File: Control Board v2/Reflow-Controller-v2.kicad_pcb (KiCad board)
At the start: 6 copper layers, 102.5 x 108 mm, 52 parts, among them J1 1366005, J2 1366005, J3 ISP, J4 Conn_01x05, J5 Conn_01x14, J6 Conn_01x04, Q1 SQ2315CES-T1_GE3, Q2 BSS127 H6327, SW1 SW_SPST, SW2 SW_Push, U2 MOC3083S-TA1, U5 ATmega328PB-A, Y2 16MHz

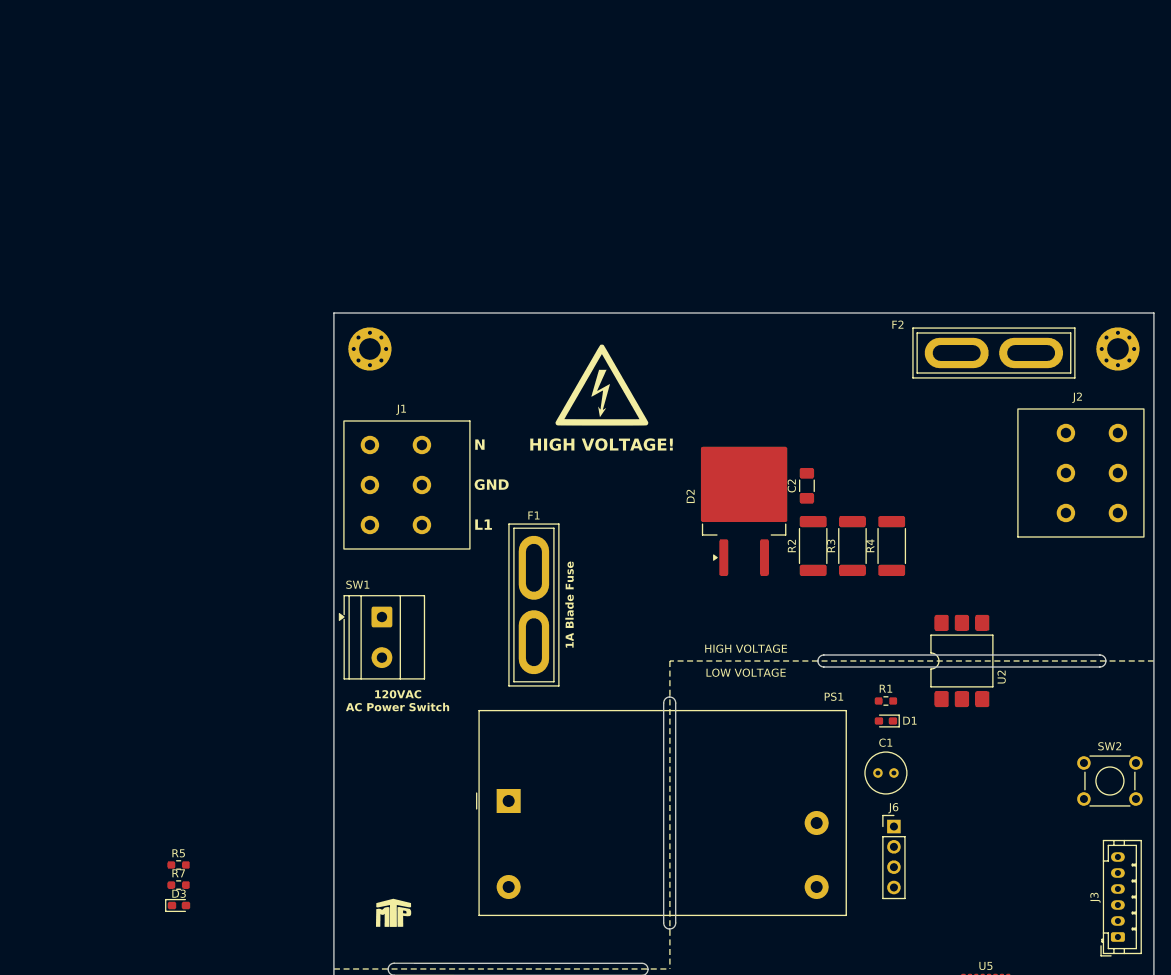
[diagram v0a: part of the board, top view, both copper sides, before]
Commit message: add silkscreen to bottom of board
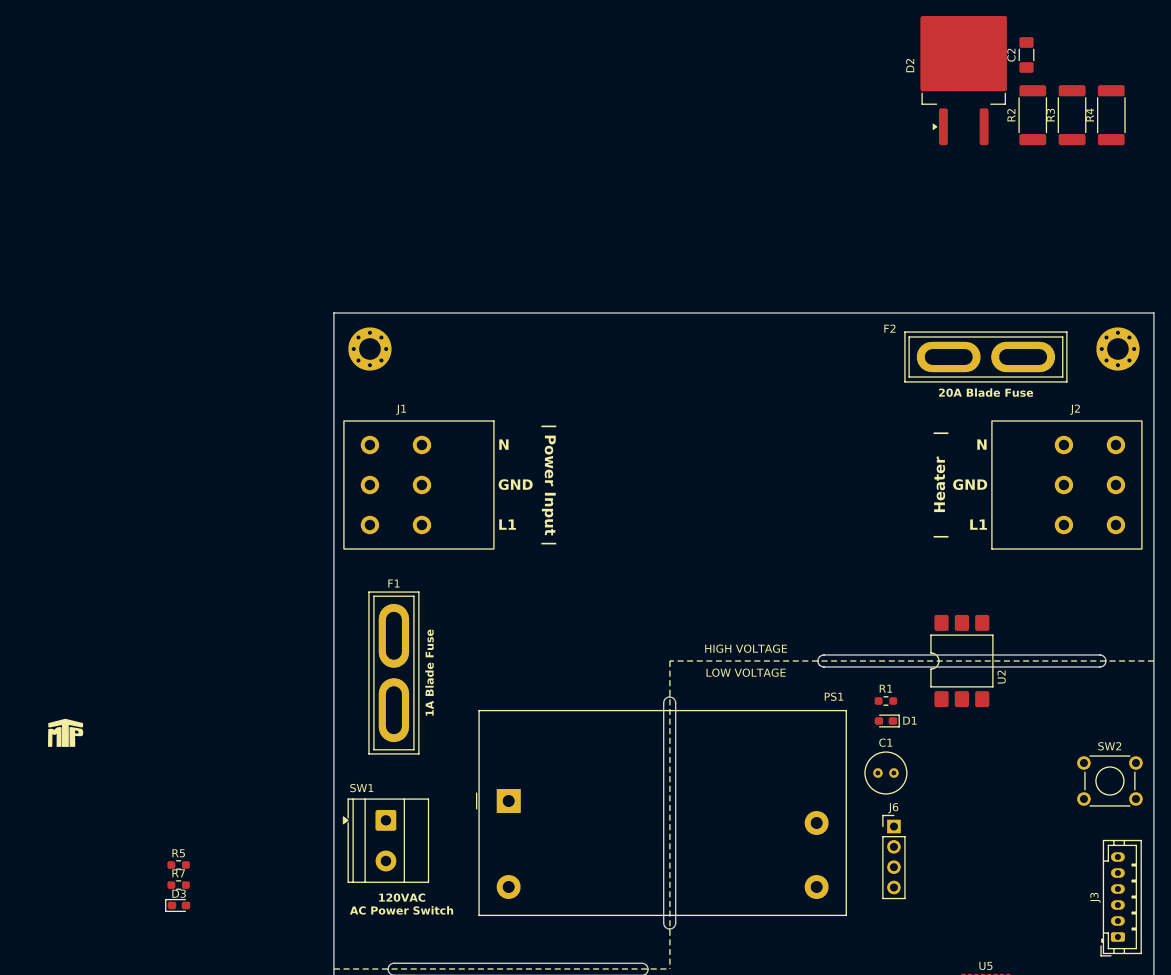
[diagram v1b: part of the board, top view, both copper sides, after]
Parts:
- G***: moved to B.Cu
- moved R4 60.4 mm to (225.7, -5.72)
- moved C2 60.4 mm to (215.1, -13.3)
- moved R2 60.4 mm to (215.9, -5.72)
- moved R3 60.4 mm to (220.8, -5.72)
- moved D2 60.4 mm to (207.2, -11.9)
- moved REF** 46.8 mm to (95.0, 72.0)
- moved SW1 25.4 mm to (135.0, 82.4)
- moved F1 19.5 mm to (136.0, 59.4)
- moved G*** 19.3 mm to (180.0, 35.0), turned to 180 degrees
- moved J2 1.52 mm to (213.0, 40.5)
- moved F2 1.12 mm to (205.3, 24.5)
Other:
- board text added: "20A Blade Fuse"
- board text added: "HIGH VOLTAGE! 120 VAC"
- board text added: "| Heater |"
- board text added: "| Power Input |"
- board text removed: "HIGH VOLTAGE!"

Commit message: change to glass fuses instead of blade fuses
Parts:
- F1: footprint Fuse:Fuse_Blade_ATO_directSolder -> Fuse:Fuseholder_Clip-5x20mm_Bel_FC-203-22_Lateral_P17.80x5.00mm_D1.17mm_Horizontal
- F2: footprint Fuse:Fuse_Blade_ATO_directSolder -> Fuse:Fuseholder_Clip-6.3x32mm_Littelfuse_122_Inline_P34.21x7.62mm_D2.54mm_Horizontal
- moved C6 185.6 mm to (219.0, 106.1)
- moved C7 185.6 mm to (219.0, 108.0)
- moved C8 185.6 mm to (219.0, 110.0)
- moved C9 185.6 mm to (219.0, 112.0)
- moved R14 185.6 mm to (217.4, 122.0)
- moved Y2 185.6 mm to (218.6, 118.7)
- moved BZ1 159.6 mm to (211.5, 90.0)
- moved TP3 120.4 mm to (179.9, 99.0)
- moved TP4 120.4 mm to (179.9, 102.5)
- moved TP7 120.4 mm to (187.0, 99.0)
- moved TP8 120.4 mm to (187.0, 102.5)
- moved D4 120.4 mm to (176.8, 105.6)
- moved R8 120.4 mm to (181.1, 105.5)
- moved TP1 120.4 mm to (176.3, 99.0)
- moved TP2 120.4 mm to (176.3, 102.5)
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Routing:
- net L1: track 0.00 -> 33.6 mm
- net /Project Architecture/AC-DC Power Supply/L1_F1_SW: track 0.00 -> 16.7 mm
- net /Project Architecture/AC-DC Power Supply/L1_F1: track 0.00 -> 15.1 mm
- net GNDPWR: track 0.00 -> 13.0 mm
- net LN: track 0.00 -> 6.50 mm
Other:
- copper layers 6 -> 4
- board text added: "1A Fuse"
- board text added: "20A Fuse"
- board text removed: "1A Blade Fuse"
- board text removed: "20A Blade Fuse"

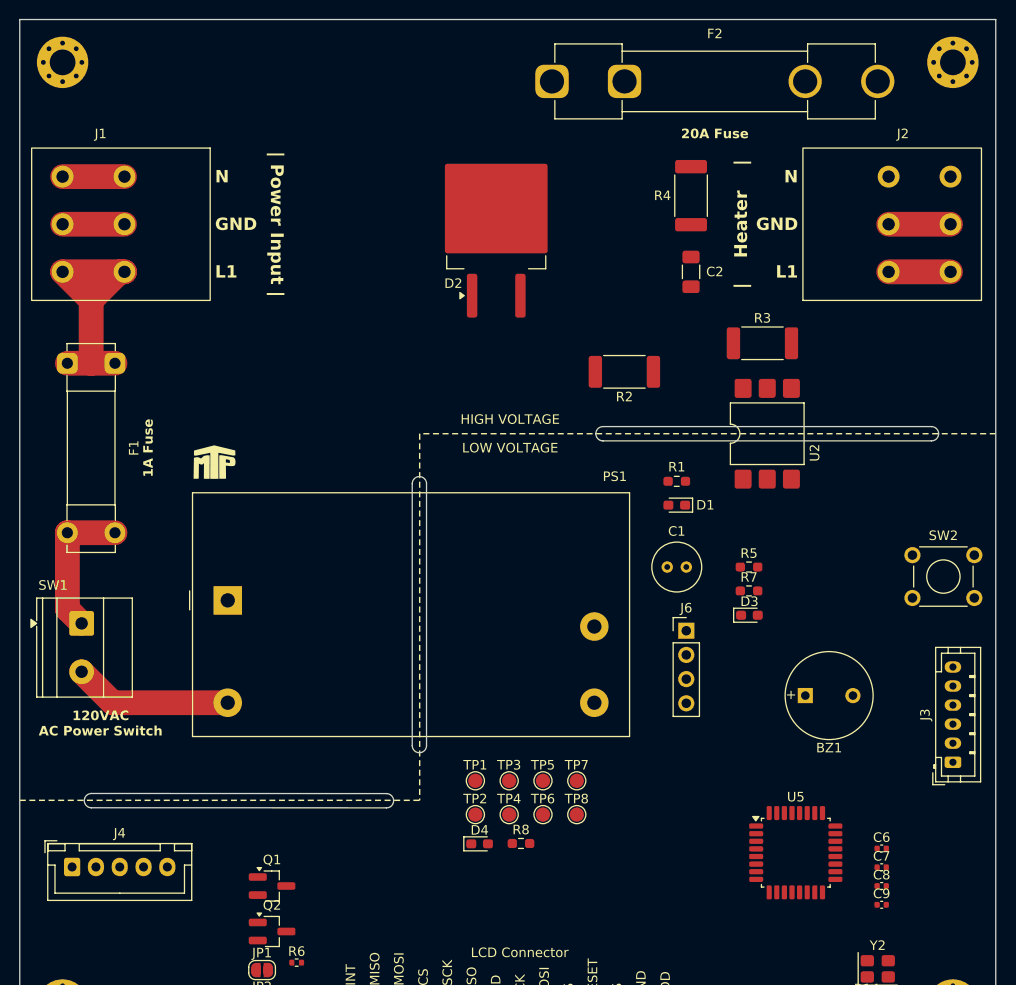
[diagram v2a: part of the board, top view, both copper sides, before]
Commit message: got most HV routed
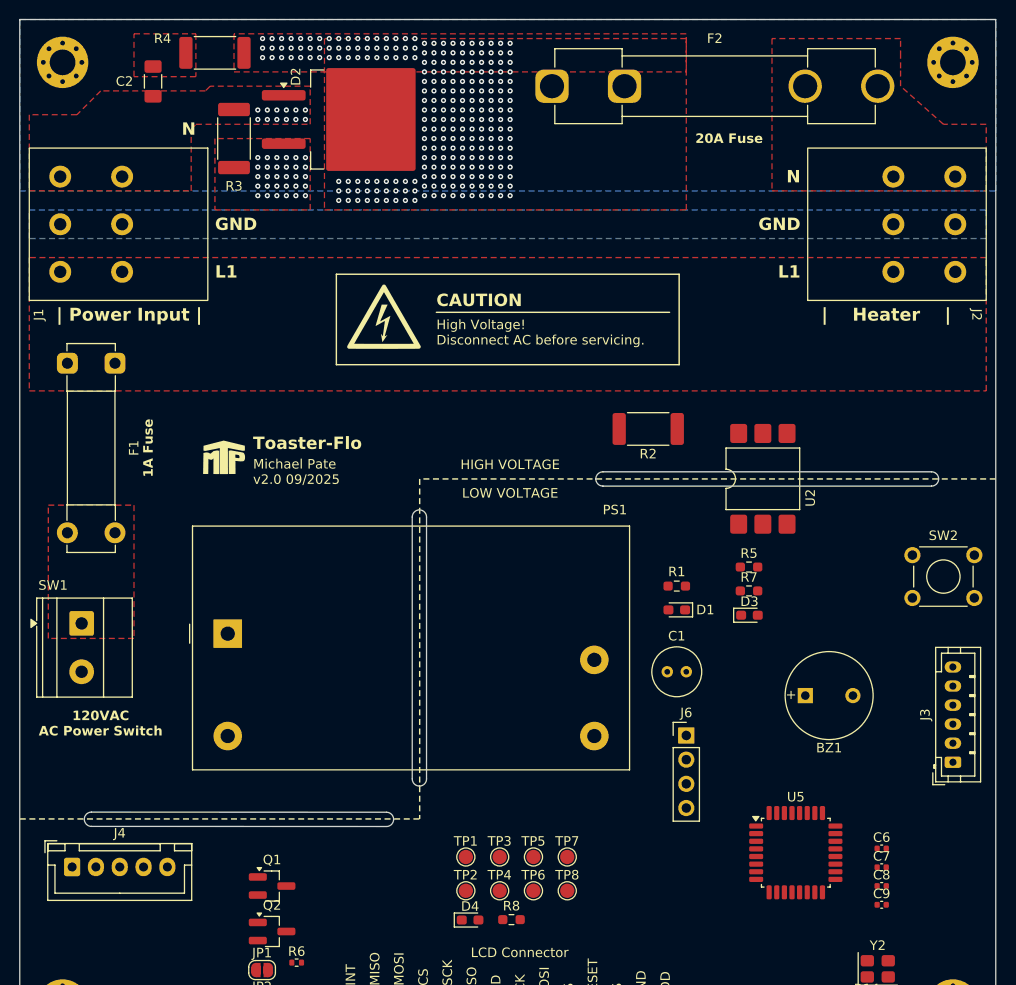
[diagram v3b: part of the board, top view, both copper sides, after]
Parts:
- added G***: LOGO, LOGO, F.Cu at (166.8, 50.2)
- moved C2 59.9 mm to (142.5, 25.5)
- moved R3 59.5 mm to (151.0, 31.5), turned to -90 degrees
- moved R4 52.2 mm to (149.0, 22.5), turned to 0 degrees
- moved D2 18.2 mm to (163.9, 29.5), turned to 0 degrees
- moved C1 11.0 mm to (196.5, 87.5)
- moved D1 11.0 mm to (197.5, 81.0)
- moved G*** 11.0 mm to (180.0, 46.0)
- moved J6 11.0 mm to (198.5, 94.2)
- moved R1 11.0 mm to (197.5, 78.5)
- moved D4 8.06 mm to (175.8, 113.6)
- moved R8 8.06 mm to (180.1, 113.5)
- moved TP1 8.06 mm to (175.3, 107.0)
- moved TP2 8.06 mm to (175.3, 110.5)
- moved TP3 8.06 mm to (178.9, 107.0)
- moved TP4 8.06 mm to (178.9, 110.5)
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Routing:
- net L1: track 33.6 -> 0.00 mm
- net /Project Architecture/AC-DC Power Supply/L1_F1_SW: track 16.7 -> 0.00 mm
- net /Project Architecture/AC-DC Power Supply/L1_F1: track 15.1 -> 0.00 mm
- net GNDPWR: track 13.0 -> 0.00 mm
- net LN: track 6.50 -> 0.00 mm, vias 0 -> 12
- net /Project Architecture/Heater Control/LN_OPTO: vias 0 -> 30
- net /Project Architecture/Heater Control/L1_F2: vias 0 -> 248
- added copper zone on B.Cu, net (none)
- added copper zone on F.Cu, net /Project Architecture/AC-DC Power Supply/L1_F1
- added copper zone on F.Cu, net /Project Architecture/Heater Control/L1_F2
- added copper zone on F.Cu, net /Project Architecture/Heater Control/L1_F2_RC
- added copper zone on F.Cu, net /Project Architecture/Heater Control/L1_HEATER
- added copper zone on F.Cu, net /Project Architecture/Heater Control/LN_OPTO
- added copper zone on B.Cu, net GNDPWR
- added copper zone on F.Cu, net L1
- added copper zone on F.Cu, net LN
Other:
- outline, holes or cut-outs redrawn
- board text added: "CAUTION"
- board text added: "High Voltage! Disconnect AC before servicing."
- board text added: "Michael Pate v2.0 09/2025"
- board text added: "Toaster-Flo"

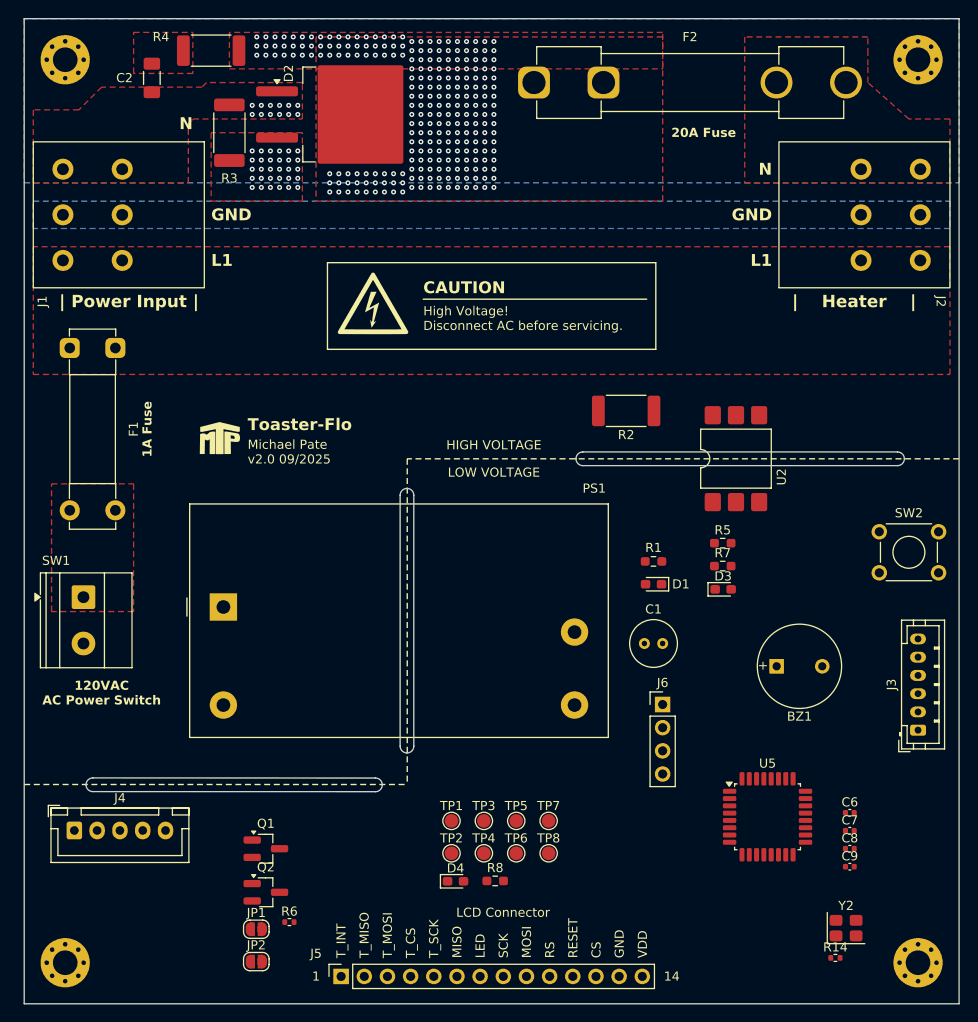
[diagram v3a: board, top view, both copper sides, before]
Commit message: add external 5v input and move stuff around on board
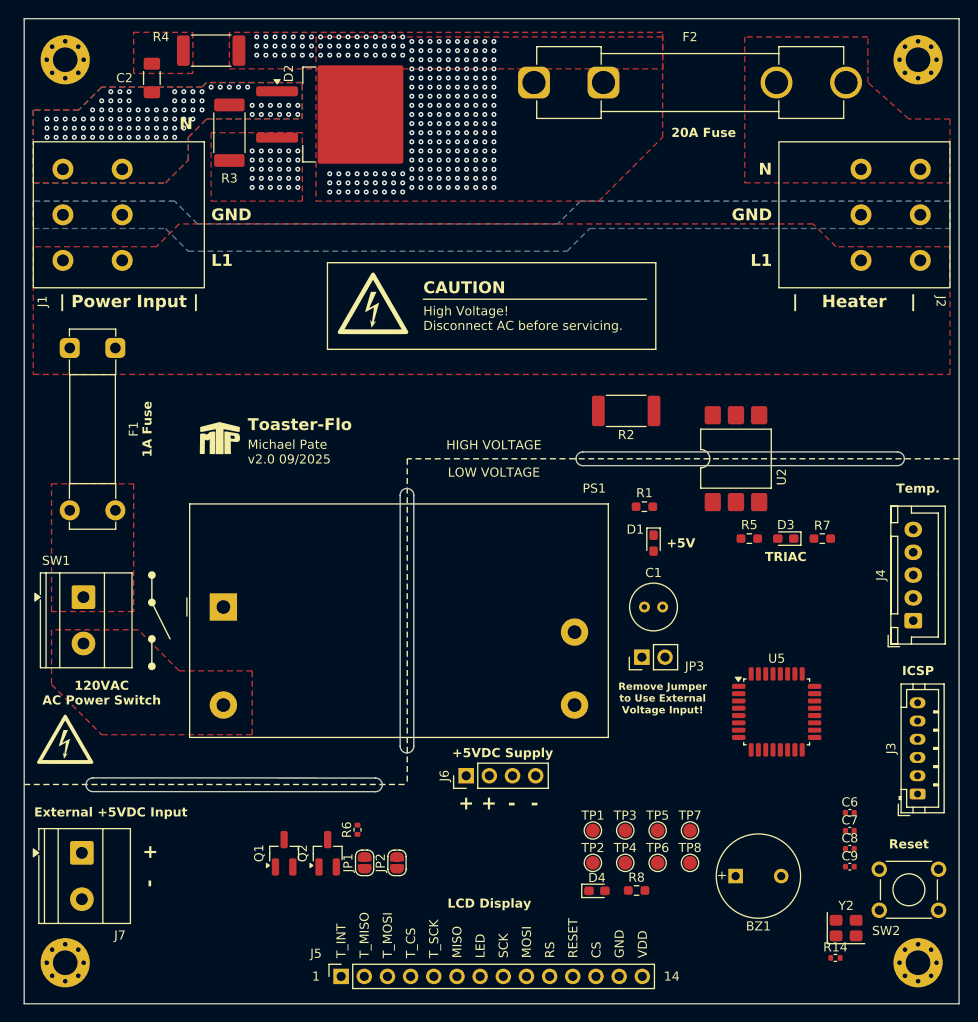
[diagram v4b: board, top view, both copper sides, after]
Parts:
- added G***: LOGO, LOGO, F.Cu at (133.0, 98.0)
- added J7: Conn_01x02, TerminalBlock_Phoenix:TerminalBlock_Phoenix_MKDS-1,5-2-5.08_1x02_P5.08mm_Horizontal, F.Cu at (134.8, 110.5)
- added JP3: Jumper_2_Open, Connector_PinHeader_2.54mm:PinHeader_1x02_P2.54mm_Vertical, F.Cu at (196.2, 89.0)
- moved J4 94.8 mm to (226.0, 85.0), turned to 90 degrees
- moved SW2 37.0 mm to (222.2, 112.2)
- moved BZ1 23.4 mm to (207.0, 113.0)
- moved J6 22.9 mm to (177.0, 102.0), turned to 90 degrees
- moved JP2 18.8 mm to (169.4, 111.5), turned to 90 degrees
- moved D4 15.5 mm to (191.3, 114.6)
- moved R8 15.5 mm to (195.6, 114.6)
- moved TP1 15.5 mm to (190.8, 108.0)
- moved TP2 15.5 mm to (190.8, 111.5)
- moved TP3 15.5 mm to (194.4, 108.0)
- moved TP4 15.5 mm to (194.4, 111.5)
- moved TP5 15.5 mm to (197.9, 108.0)
- moved TP6 15.5 mm to (197.9, 111.5)
- moved TP7 15.5 mm to (201.5, 108.0)
- moved TP8 15.5 mm to (201.5, 111.5)
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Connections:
- PS1 pad 4: VDD -> /Project Architecture/AC-DC Power Supply/VDD_AC_DC
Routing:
- net LN: vias 12 -> 93
- added copper zone on F.Cu, net /Project Architecture/AC-DC Power Supply/L1_F1_SW
- added copper zone on B.Cu, net LN
- removed copper zone on B.Cu, net (none)
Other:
- board text added: "+"
- board text added: "+ -"
- board text added: "+5V"
- board text added: "+5VDC Supply"
- board text added: "-"
- board text added: "External +5VDC Input"
- board text added: "ICSP"
- board text added: "LCD Display"
- board text added: "Remove Jumper to Use External Voltage Input!"
- board text added: "Reset"
- board text added: "TRIAC"
- board text added: "Temp."
- board text removed: "LCD Connector"

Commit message: change silkscreen
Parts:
- moved G*** 0.50 mm to (132.5, 98.0)
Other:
- board text added: "AC Power Switch"
- board text added: "CAUTION - 115VAC"
- board text added: "High Voltage! Remove AC during programming!"
- board text added: "PROTOTYPE"
- board text added: "USE 120VAC RATED SWITCH"
- board text removed: "120VAC AC Power Switch"
- board text removed: "CAUTION"
- board text removed: "High Voltage! Disconnect AC before servicing."
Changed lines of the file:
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@@
 		(tags "resistor handsolder")
 		(property "Reference" "R3"
-			(at 5 0 180)
+			(at -0.239713 3.377104 180)
 			(layer "F.SilkS")
 			(effects
@@
 	(footprint "LOGO"
 		(layer "F.Cu")
-		(at 133 98)
+		(at 132.5 98)
 		(property "Reference" "G***"
 			(at 0 0 0)
@@
 	(gr_line
 		(start 172.25 49.75)
-		(end 196.75 49.75)
+		(end 197.5 49.75)
 		(stroke
 			(width 0.15)
@@
 	(gr_rect
 		(start 161.75 45.75)
-		(end 197.75 55.25)
+		(end 198.75 55.25)
 		(stroke
 			(width 0.15)
@@
 		)
 	)
-	(gr_text "CAUTION"
+	(gr_text "CAUTION - 115VAC"
 		(at 172.25 49.25 0)
 		(layer "F.SilkS")
@@
 	)
 	(gr_text "N"
-		(at 145.5 30.5 0)
+		(at 149 37.5 0)
 		(layer "F.SilkS")
 		(effects
@@
 		)
 	)
+	(gr_text "PROTOTYPE"
+		(at 158.5 60.5 0)
+		(layer "F.SilkS" knockout)
+		(effects
+			(font
+				(size 1.35 1.35)
+				(thickness 0.27)
+				(bold yes)
+			)
+		)
+	)
 	(gr_text "GND"
 		(at 210.5 40.5 0)
@@
 		)
 	)
-	(gr_text "120VAC\nAC Power Switch"
-		(at 137 92.92 0)
+	(gr_text "AC Power Switch"
+		(at 136.5 92.5 0)
 		(layer "F.SilkS")
 		(effects
@@
 		)
 	)
+	(gr_text "USE 120VAC\nRATED SWITCH"
+		(at 141 98 0)
+		(layer "F.SilkS")
+		(effects
+			(font
+				(size 1 1)
+				(thickness 0.2)
+				(bold yes)
+			)
+		)
+	)
 	(gr_text "14"
 		(at 199.5 124 0)
@@
 		)
 	)
-	(gr_text "High Voltage!\nDisconnect AC before servicing."
+	(gr_text "High Voltage!\nRemove AC during programming!"
 		(at 172.25 53.25 0)
 		(layer "F.SilkS")
